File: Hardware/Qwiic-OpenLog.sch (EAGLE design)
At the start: 30 parts, among them J2 SMD, J3 PTH, J4 SMD, J5 ISP, Q1 16MHZ, U2 ATMEGA328P, U3 microSD Socket

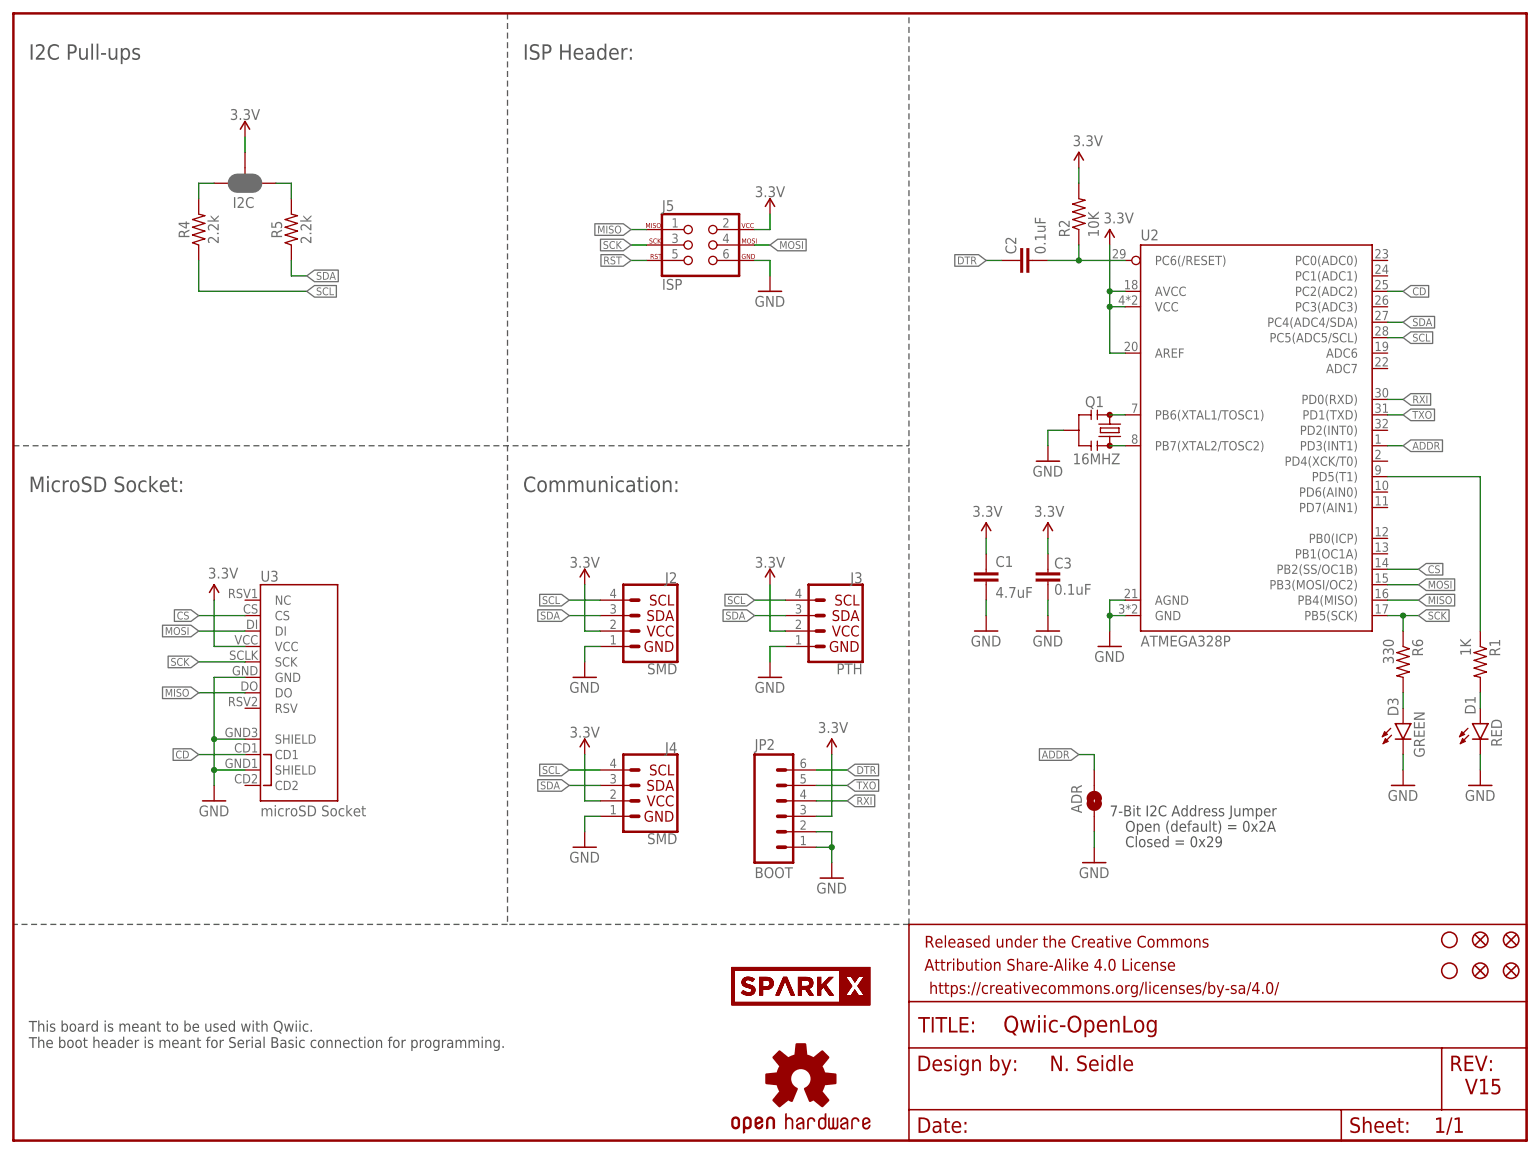
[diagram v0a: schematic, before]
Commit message: Updating with Buzzard labels
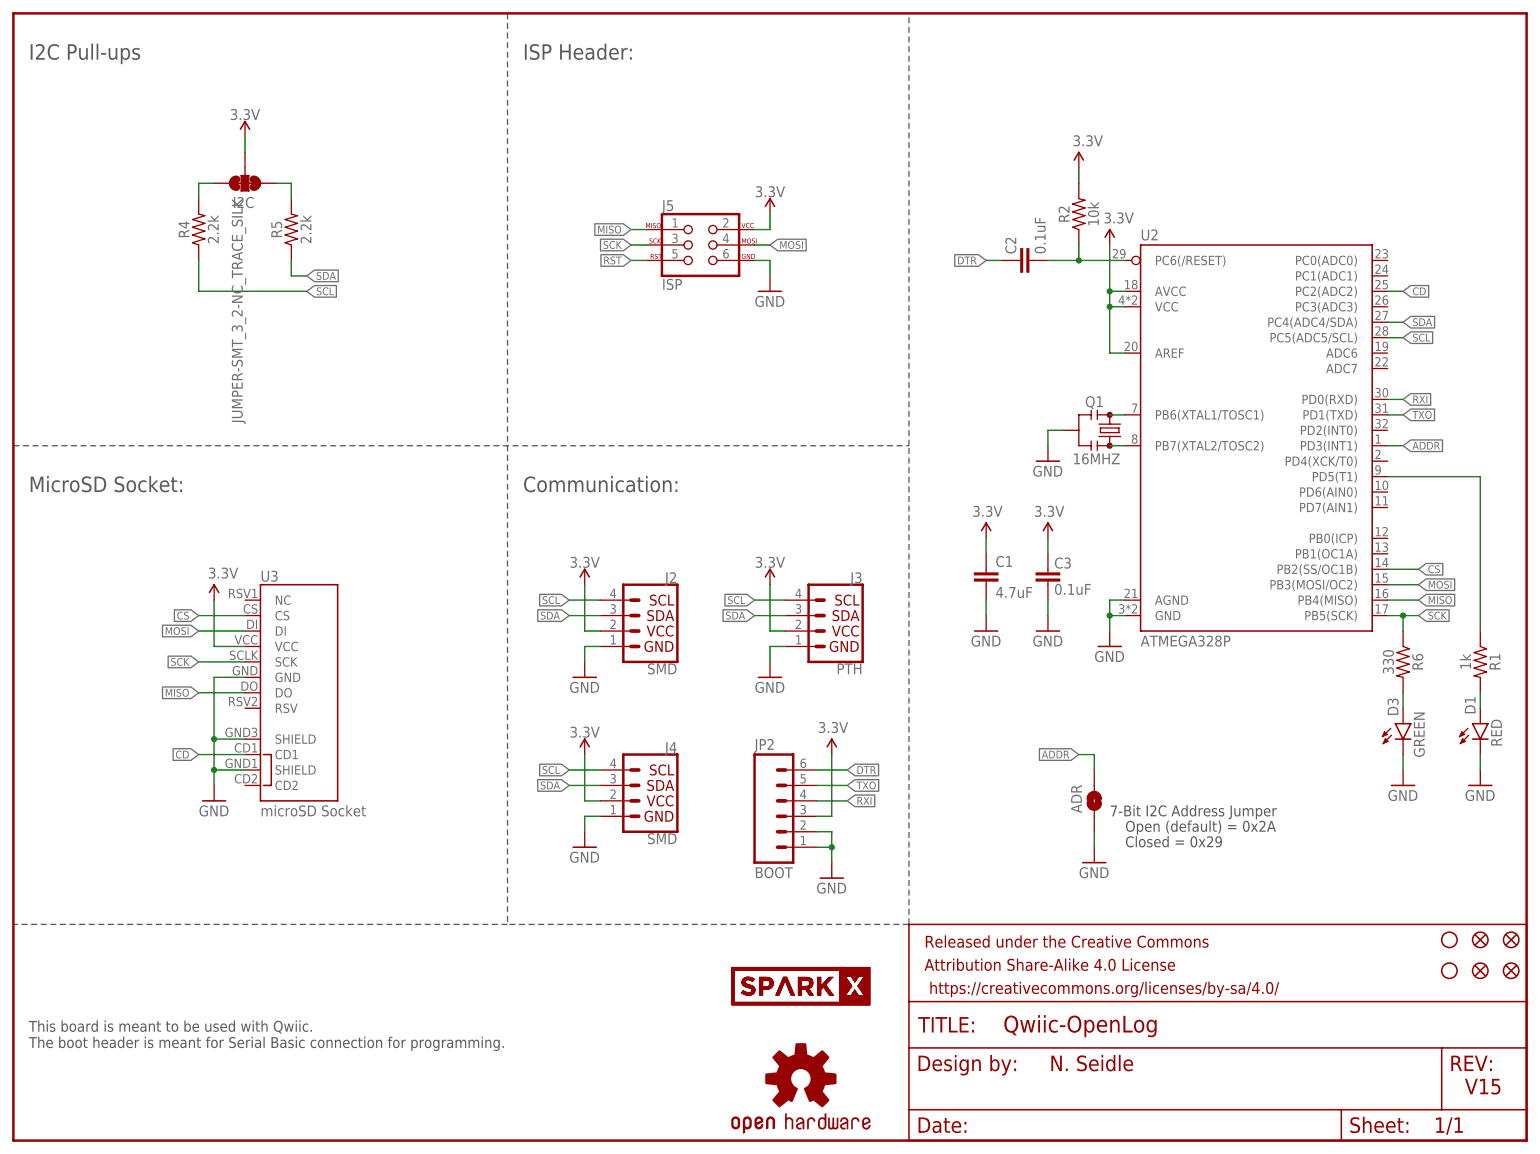
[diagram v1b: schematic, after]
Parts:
- C1: device SparkFun-Capacitors:4.7UF0603 -> SparkFun-Capacitors:4.7UF-0603-6.3V-(10%)
- C2, C3: device SparkFun-Capacitors:0.1UF-25V(+80/-20%)(0603) -> SparkFun-Capacitors:0.1UF-0603-25V-(+80/-20%)
- I2C: value JUMPER-SMT_3_2-NC_PASTE_SILK -> JUMPER-SMT_3_2-NC_TRACE_SILK; device SparkFun-Jumpers:JUMPER-SMT_3_2-NC_PASTE_SILK -> SparkFun-Jumpers:JUMPER-SMT_3_2-NC_TRACE_SILK
- R1: value 1K -> 1k; device SparkFun-Resistors:1KOHM-1/10W-1%(0603) -> SparkFun-Resistors:1KOHM-0603-1/10W-1%
- R2: value 10K -> 10k; device SparkFun-Resistors:10KOHM-1/10W-1%(0603)0603 -> SparkFun-Resistors:10KOHM-0603-1/10W-1%
- R6: device SparkFun-Resistors:330OHM1/10W1%(0603) -> SparkFun-Resistors:330OHM-0603-1/10W-1%
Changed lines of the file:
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@@
 <?xml version="1.0" encoding="utf-8"?>
 <!DOCTYPE eagle SYSTEM "eagle.dtd">
-<eagle version="7.7.0">
+<eagle version="9.1.1">
 <drawing>
 <settings>
-<setting alwaysvectorfont="no"/>
+<setting alwaysvectorfont="yes"/>
+<setting keepoldvectorfont="yes"/>
 <setting verticaltext="up"/>
 </settings>
@@
 <parts>
 <part name="FRAME1" library="SparkFun-Aesthetics" deviceset="FRAME-LETTER" device=""/>
-<part name="R2" library="SparkFun-Resistors" deviceset="10KOHM-1/10W-1%(0603)" device="0603" value="10K"/>
-<part name="C3" library="SparkFun-Capacitors" deviceset="0.1UF-25V(+80/-20%)(0603)" device="" value="0.1uF"/>
+<part name="R2" library="SparkFun-Resistors" deviceset="10KOHM" device="-0603-1/10W-1%" value="10k"/>
+<part name="C3" library="SparkFun-Capacitors" deviceset="0.1UF" device="-0603-25V-(+80/-20%)" value="0.1uF"/>
 <part name="GND1" library="SparkFun" deviceset="GND" device=""/>
-<part name="R6" library="SparkFun-Resistors" deviceset="330OHM1/10W1%(0603)" device="" value="330"/>
+<part name="R6" library="SparkFun-Resistors" deviceset="330OHM" device="-0603-1/10W-1%" value="330"/>
 <part name="D3" library="SparkFun-LED" deviceset="LED-GREEN" device="0603" value="GREEN"/>
 <part name="GND8" library="SparkFun" deviceset="GND" device=""/>
@@
 <part name="P+1" library="SparkFun" deviceset="3.3V" device=""/>
 <part name="GND5" library="SparkFun" deviceset="GND" device=""/>
-<part name="C2" library="SparkFun-Capacitors" deviceset="0.1UF-25V(+80/-20%)(0603)" device="" value="0.1uF"/>
+<part name="C2" library="SparkFun-Capacitors" deviceset="0.1UF" device="-0603-25V-(+80/-20%)" value="0.1uF"/>
 <part name="U3" library="SparkFun-Connectors" deviceset="MICRO_SD_SOCKET" device="NEW" value="microSD Socket"/>
-<part name="R1" library="SparkFun-Resistors" deviceset="1KOHM-1/10W-1%(0603)" device="" value="1K"/>
+<part name="R1" library="SparkFun-Resistors" deviceset="1KOHM" device="-0603-1/10W-1%" value="1k"/>
 <part name="D1" library="SparkFun-LED" deviceset="LED-RED" device="0603" value="RED"/>
 <part name="GND2" library="SparkFun" deviceset="GND" device=""/>
@@
 <part name="J4" library="SparkFun-Connectors" deviceset="QWIIC_CONNECTOR" device="JS-1MM" value="SMD"/>
 <part name="GND13" library="SparkFun" deviceset="GND" device=""/>
-<part name="C1" library="SparkFun-Capacitors" deviceset="4.7UF" device="0603" value="4.7uF"/>
+<part name="C1" library="SparkFun-Capacitors" deviceset="4.7UF" device="-0603-6.3V-(10%)" value="4.7uF"/>
 <part name="P+3" library="SparkFun" deviceset="3.3V" device=""/>
 <part name="GND7" library="SparkFun" deviceset="GND" device=""/>
@@
 <part name="R4" library="SparkFun-Resistors" deviceset="2.2KOHM" device="-0603-1/10W-1%" value="2.2k"/>
 <part name="R5" library="SparkFun-Resistors" deviceset="2.2KOHM" device="-0603-1/10W-1%" value="2.2k"/>
-<part name="I2C" library="SparkFun-Jumpers" deviceset="JUMPER-SMT_3_2-NC_PASTE" device="_SILK" value=""/>
+<part name="I2C" library="SparkFun-Jumpers" deviceset="JUMPER-SMT_3_2-NC_TRACE" device="_SILK" value="JUMPER-SMT_3_2-NC_TRACE_SILK"/>
 <part name="SUPPLY1" library="SparkFun-PowerSymbols" deviceset="3.3V" device=""/>
 <part name="U$2" library="SparkX" deviceset="SPARKX-LOGO" device="3" value="SPARKX-LOGO3"/>

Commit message: Adding pull up on CS pin to allow for easier ISP programming.
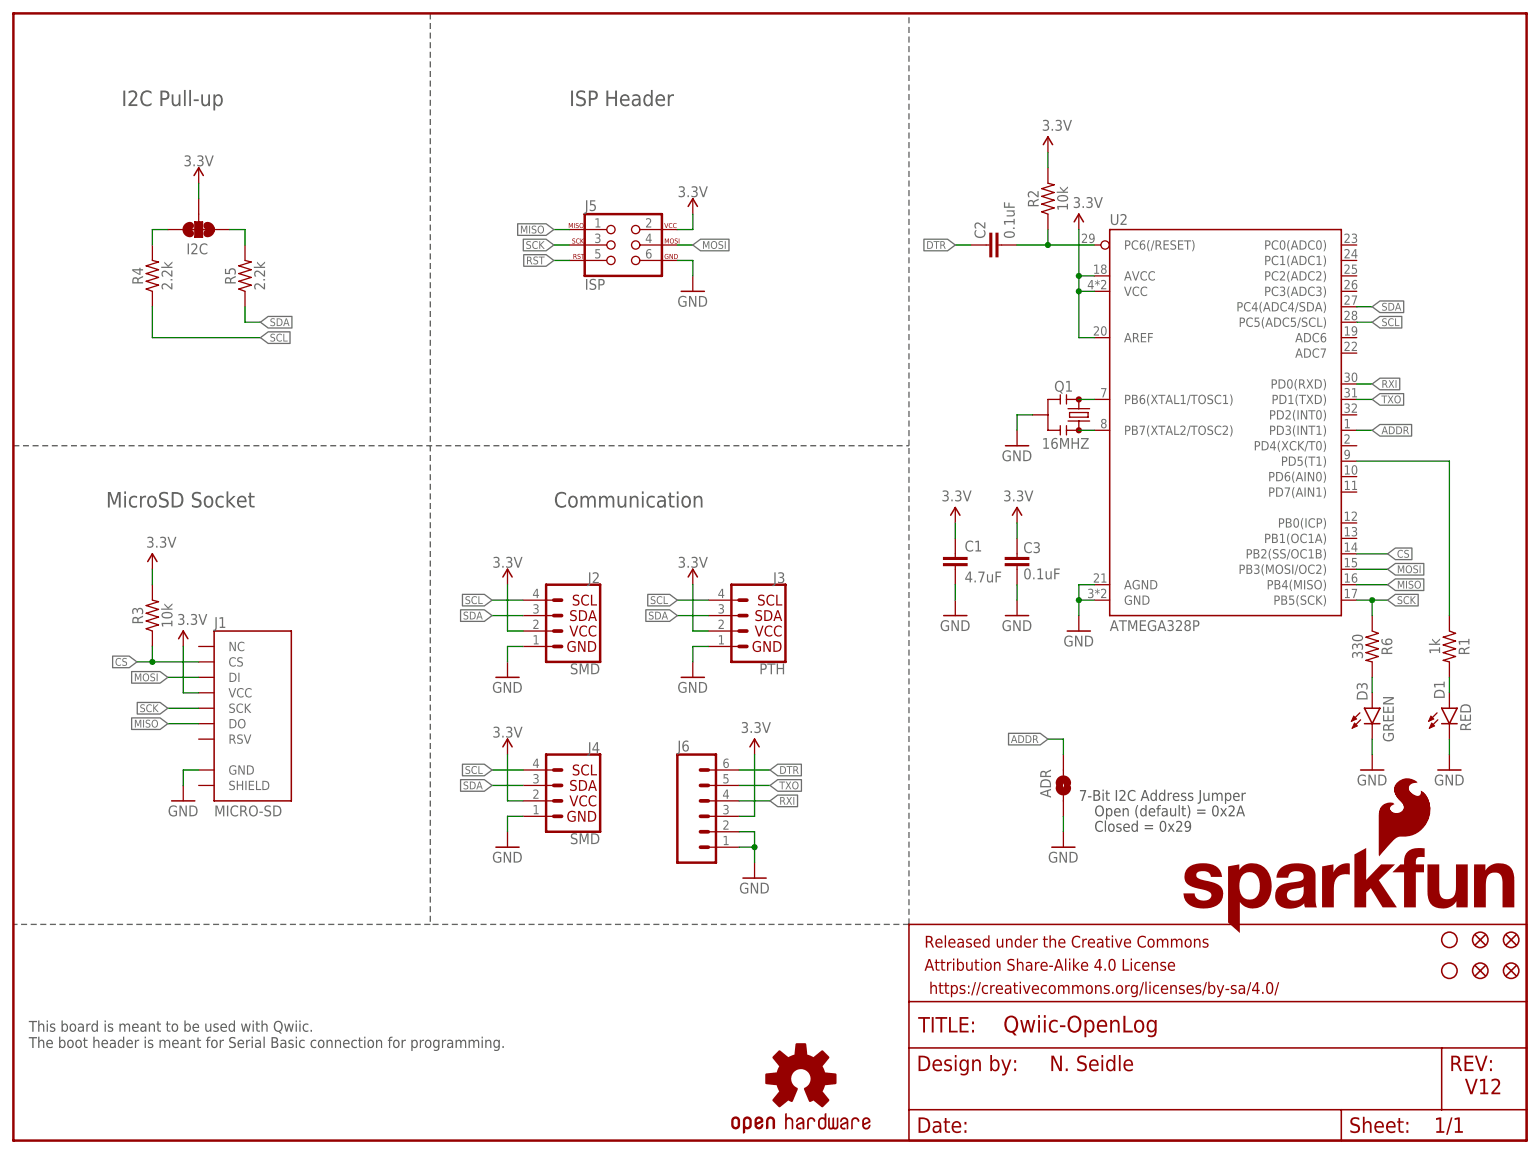
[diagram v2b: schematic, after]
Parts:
- removed JP2: BOOT, SparkFun-Connectors:M06NO_SILK_FEMALE_PTH
- removed U$1: SPARKX-LOGO4, SparkX:SPARKX-LOGO4
- removed U$2: SPARKX-LOGO3, SparkX:SPARKX-LOGO3
- removed U3: microSD Socket, SparkFun-Connectors:MICRO_SD_SOCKETNEW
- added J1: MICRO-SD, SparkFun-Connectors:MICRO-SD_CARD_SOCKETPUSH-PUSH
- added J6: (no value), SparkFun-Connectors:CONN_06NO_SILK_NO_POP
- added LOGO1: SFE_LOGO_FLAME.1_INCH, SparkFun-Aesthetics:SFE_LOGO_FLAME.1_INCH
- added LOGO4: SFE_LOGO_NAME_FLAME.1_INCH, SparkFun-Aesthetics:SFE_LOGO_NAME_FLAME.1_INCH
- added R3: 10k, SparkFun-Resistors:10KOHM-0603-1/10W-1%
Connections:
- removed net CD: U2.PC2(ADC2), U3.CD1
- net 3.3V: now also J1.VCC, J6.3, R3.2; no longer JP2.3, U3.VCC
- net CS: now also J1.CS, R3.1; no longer U3.CS
- net DTR: now also J6.6; no longer JP2.6
- net GND: now also J1.GND, J6.1, J6.2; no longer JP2.1, JP2.2, U3.GND, U3.SHIELD@1, U3.SHIELD@3
- net MISO: now also J1.DO; no longer U3.DO
- net MOSI: now also J1.DI; no longer U3.DI
- net RXI: now also J6.4; no longer JP2.4
- net SCK: now also J1.SCK; no longer U3.SCK
- net TXO: now also J6.5; no longer JP2.5
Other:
- note added: "Communication"
- note added: "I2C Pull-up"
- note added: "ISP Header"
- note added: "MicroSD Socket"
- note added: "V12"
- note removed: "Communication:"
- note removed: "I2C Pull-ups"
- note removed: "ISP Header:"
- note removed: "MicroSD Socket:"
- note removed: "V15"
- moved on the sheet: ADR, C1, C2, C3, D1, D3, I2C, J2, J3, J4, J5, Q1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
